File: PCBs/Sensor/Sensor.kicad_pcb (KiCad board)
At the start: 2 copper layers, 35 x 45 mm, 7 parts, among them J1 RJ45, J2 RJ45, U1 ATtiny85-20P

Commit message: added info text
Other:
- board text added: "Laser-Parkour Sensor Rev. 01 © 2024 Manuel König HHN HTWG x42.space"
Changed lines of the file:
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@@
 	)
 	(paper "A4")
+	(title_block
+		(title "Laser-Parkour Sensor")
+		(date "2024-08-24")
+		(rev "01")
+		(company "Manuel König HHN HTWG x42.space")
+	)
 	(layers
 		(0 "F.Cu" signal)
@@
 		(layer "Edge.Cuts")
 	)
+	(gr_text "Laser-Parkour Sensor Rev. 01\n© 2024 Manuel König HHN HTWG\nx42.space "
+		(at 65 92.5 270)
+		(layer "B.SilkS")
+		(effects
+			(font
+				(size 1.5 1.5)
+				(thickness 0.3)
+				(bold yes)
+			)
+			(justify left bottom mirror)
+		)
+	)
 	(segment

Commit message: update footprint
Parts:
- J1, J2: footprint Sensor:WR-MJ Modular Jack Horizontal Shielded w. EMI Panel Finger 8P8C Tab Up -> Library:WR-MJ Modular Jack Horizontal Shielded w. EMI Panel Finger 8P8C Tab Up
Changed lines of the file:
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@@
 		)
 	)
-	(footprint "Sensor:WR-MJ Modular Jack Horizontal Shielded w. EMI Panel Finger 8P8C Tab Up"
+	(footprint "Library:WR-MJ Modular Jack Horizontal Shielded w. EMI Panel Finger 8P8C Tab Up"
 		(layer "F.Cu")
 		(at 76.015 84.705 90)
 		(descr "WR-MJ Modular Jack Horizontal Shielded w. EMI Panel Finger 8P8C Tab Up")
 		(property "Reference" "J2"
-			(at -8.15 -9.015 90)
+			(at 10.1925 -6.485 90)
 			(unlocked yes)
 			(layer "F.SilkS")
@@
 		)
 		(property "Value" "RJ45"
-			(at -8.2325 -6.5575 90)
+			(at 10.11 -4.0275 90)
 			(unlocked yes)
 			(layer "F.Fab")
@@
 			)
 		)
-		(property "Footprint" "Sensor:WR-MJ Modular Jack Horizontal Shielded w. EMI Panel Finger 8P8C Tab Up"
+		(property "Footprint" "Library:WR-MJ Modular Jack Horizontal Shielded w. EMI Panel Finger 8P8C Tab Up"
 			(at 0 0 90)
 			(layer "F.Fab")
@@
 		)
 	)
-	(footprint "Sensor:WR-MJ Modular Jack Horizontal Shielded w. EMI Panel Finger 8P8C Tab Up"
+	(footprint "Library:WR-MJ Modular Jack Horizontal Shielded w. EMI Panel Finger 8P8C Tab Up"
 		(layer "F.Cu")
 		(at 76.015 63.705 90)
 		(descr "WR-MJ Modular Jack Horizontal Shielded w. EMI Panel Finger 8P8C Tab Up")
 		(property "Reference" "J1"
-			(at -8.0675 -8.9725 90)
+			(at 10.1925 -6.485 90)
 			(unlocked yes)
 			(layer "F.SilkS")
@@
 		)
 		(property "Value" "RJ45"
-			(at -8.15 -6.515 90)
+			(at 10.11 -4.0275 90)
 			(unlocked yes)
 			(layer "F.Fab")
@@
 			)
 		)
-		(property "Footprint" "Sensor:WR-MJ Modular Jack Horizontal Shielded w. EMI Panel Finger 8P8C Tab Up"
+		(property "Footprint" "Library:WR-MJ Modular Jack Horizontal Shielded w. EMI Panel Finger 8P8C Tab Up"
 			(at 0 0 90)
 			(layer "F.Fab")

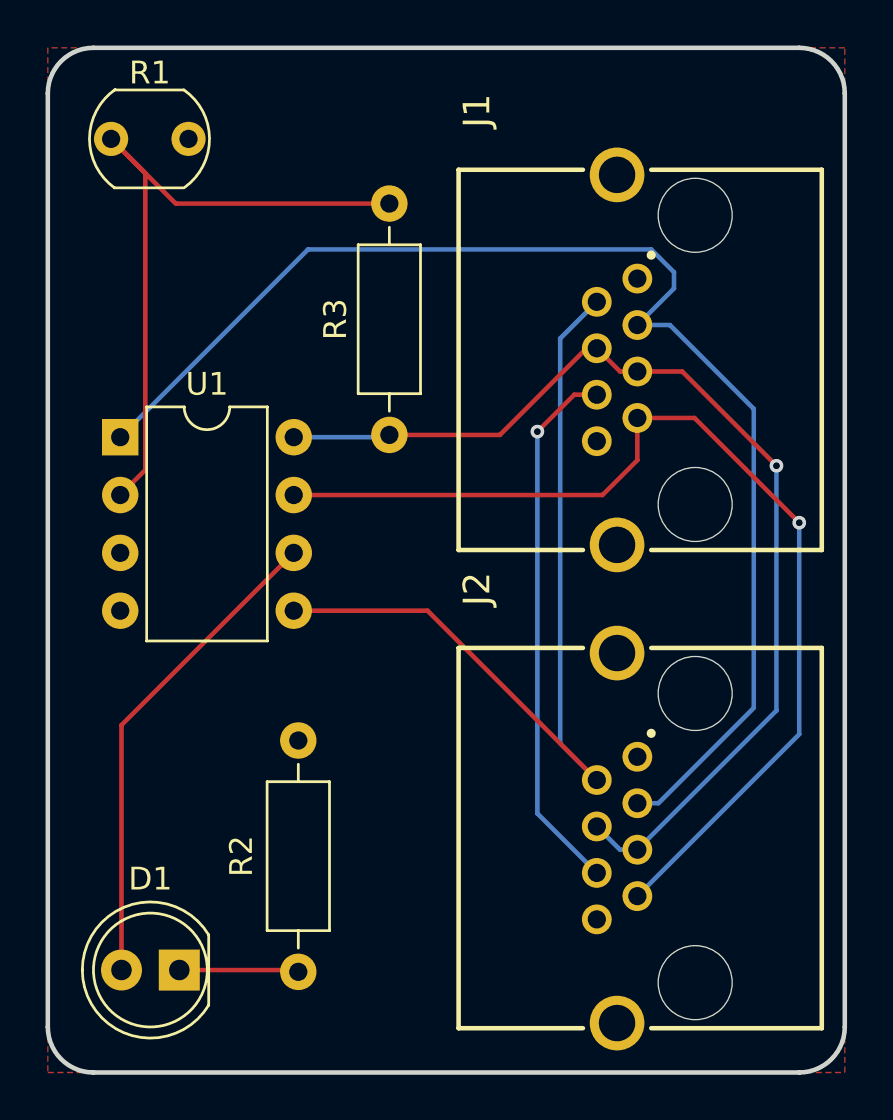
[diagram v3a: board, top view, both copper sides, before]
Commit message: integrate buzzer PCB into Sensor
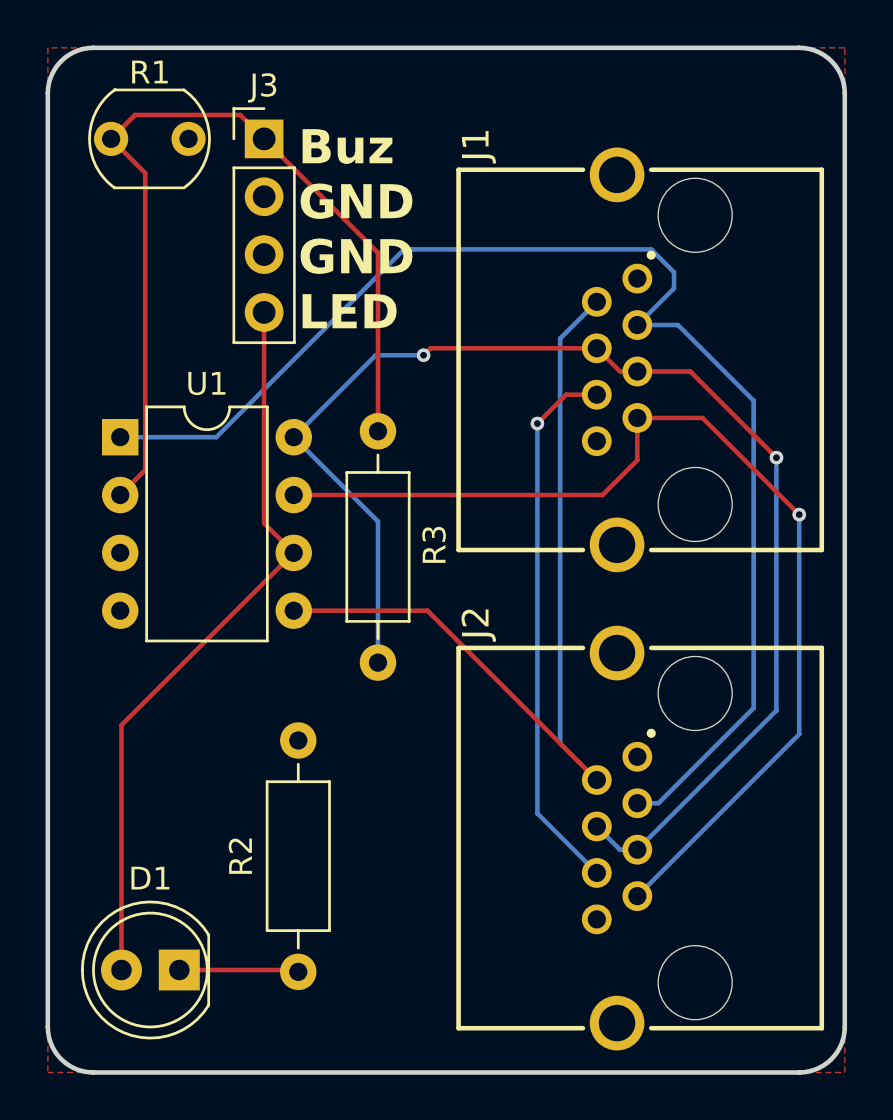
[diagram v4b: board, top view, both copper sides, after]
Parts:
- added J3: Conn_01x04_Pin, Connector_PinHeader_2.54mm:PinHeader_1x04_P2.54mm_Vertical, F.Cu at (59.5, 54.0)
- moved R3 10.0 mm to (64.5, 77.0)
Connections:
- net Net-(D1-A) renamed /out
- net Net-(U1-XTAL1/PB3) renamed /in
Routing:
- net +5V: track 46.5 -> 57.8 mm, vias 1 -> 2
- net /out: track 21.5 -> 32.6 mm
- net /in: track 30.1 -> 39.2 mm
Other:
- board text added: "Buz GND GND LED"

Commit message: Update README
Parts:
- D1: value green -> LED
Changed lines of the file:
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@@
 			)
 		)
-		(property "Value" "green"
+		(property "Value" "LED"
 			(at 1.275 -3.5 0)
 			(layer "F.Fab")

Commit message: added jumper pad
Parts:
- added JP1: Jumper_2_Open, Jumper:SolderJumper-2_P1.3mm_Open_TrianglePad1.0x1.5mm, B.Cu at (56.8, 83.5)
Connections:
- U1 pad 3: unconnected-(U1-XTAL2/PB4-Pad3) -> Net-(JP1-A)
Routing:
- net Net-(JP1-B): track 24.0 -> 38.0 mm
- net Net-(JP1-A): track 0.00 -> 12.5 mm
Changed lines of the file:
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@@
 	(net 2 "/out")
 	(net 3 "+5V")
-	(net 4 "Net-(J1-Pad6)")
+	(net 4 "Net-(JP1-B)")
 	(net 5 "GND")
 	(net 6 "/SDA")
@@
 	(net 8 "/SCL")
 	(net 9 "/in")
-	(net 10 "unconnected-(U1-XTAL2{slash}PB4-Pad3)")
+	(net 10 "Net-(JP1-A)")
 	(footprint "OptoDevice:R_LDR_5.1x4.3mm_P3.4mm_Vertical"
 		(layer "F.Cu")
@@
 			(layers "*.Cu" "*.Mask")
 			(remove_unused_layers no)
-			(net 4 "Net-(J1-Pad6)")
+			(net 4 "Net-(JP1-B)")
 			(pintype "passive")
 			(solder_mask_margin 0.1016)
@@
 			(layers "*.Cu" "*.Mask")
 			(remove_unused_layers no)
-			(net 4 "Net-(J1-Pad6)")
+			(net 4 "Net-(JP1-B)")
 			(pintype "passive")
 			(solder_mask_margin 0.1016)
@@
 			(layers "*.Cu" "*.Mask")
 			(remove_unused_layers no)
-			(net 10 "unconnected-(U1-XTAL2{slash}PB4-Pad3)")
+			(net 10 "Net-(JP1-A)")
 			(pinfunction "XTAL2/PB4")
-			(pintype "bidirectional+no_connect")
+			(pintype "bidirectional")
 		)
 		(pad "4" thru_hole oval
@@
 			(rotate
 				(xyz 0 0 0)
+			)
+		)
+	)
+	(footprint "Jumper:SolderJumper-2_P1.3mm_Open_TrianglePad1.0x1.5mm"
+		(layer "B.Cu")
+		(at 56.775 83.5)
+		(descr "SMD Solder Jumper, 1x1.5mm Triangular Pads, 0.3mm gap, open")
+		(tags "solder jumper open")
+		(property "Reference" "JP1"
+			(at 0 1.8 360)
+			(layer "B.SilkS")
+			(effects
+				(font
+					(size 1 1)
+					(thickness 0.15)
+				)
+				(justify mirror)
+			)
+		)
+		(property "Value" "Jumper_2_Open"
+			(at 0 -1.9 360)
+			(layer "B.Fab")
+			(effects
+				(font
+					(size 1 1)
+					(thickness 0.15)
+				)
+				(justify mirror)
+			)
+		)
+		(property "Footprint" "Jumper:SolderJumper-2_P1.3mm_Open_TrianglePad1.0x1.5mm"
+			(at 0 0 180)
+			(unlocked yes)
+			(layer "B.Fab")
+			(hide yes)
+			(effects
+				(font
+					(size 1.27 1.27)
+					(thickness 0.15)
+				)
+				(justify mirror)
+			)
+		)
+		(property "Datasheet" ""
+			(at 0 0 180)
+			(unlocked yes)
+			(layer "B.Fab")
+			(hide yes)
+			(effects
+				(font
+					(size 1.27 1.27)
+					(thickness 0.15)
+				)
+				(justify mirror)
+			)
+		)
+		(property "Description" "Jumper, 2-pole, open"
+			(at 0 0 180)
+			(unlocked yes)
+			(layer "B.Fab")
+			(hide yes)
+			(effects
+				(font
+					(size 1.27 1.27)
+					(thickness 0.15)
+				)
+				(justify mirror)
+			)
+		)
+		(property ki_fp_filters "Jumper* TestPoint*2Pads* TestPoint*Bridge*")
+		(sheetname "Root")
+		(sheetfile "Sensor.kicad_sch")
+		(zone_connect 1)
+		(attr exclude_from_pos_files)
+		(fp_line
+			(start -1.4 -1)
+			(end 1.4 -1)
+			(stroke
+				(width 0.12)
+				(type solid)
+			)
+			(layer "B.SilkS")
+		)
+		(fp_line
+			(start -1.4 1)
+			(end -1.4 -1)
+			(stroke
+				(width 0.12)
+				(type solid)
+			)
+			(layer "B.SilkS")
+		)
+		(fp_line
+			(start 1.4 -1)
+			(end 1.4 1)
+			(stroke
+				(width 0.12)
+				(type solid)
+			)
+			(layer "B.SilkS")
+		)
+		(fp_line
+			(start 1.4 1)
+			(end -1.4 1)
+			(stroke
+				(width 0.12)
+				(type solid)
+			)
+			(layer "B.SilkS")
+		)
+		(fp_line
+			(start -1.65 -1.25)
+			(end -1.65 1.25)
+			(stroke
+				(width 0.05)
+				(type solid)
+			)
+			(layer "B.CrtYd")
+		)
+		(fp_line
+			(start -1.65 -1.25)
+			(end 1.65 -1.25)
+			(stroke
+				(width 0.05)
+				(type solid)
+			)
+			(layer "B.CrtYd")
+		)
+		(fp_line
+			(start 1.65 1.25)
+			(end -1.65 1.25)
+			(stroke
+				(width 0.05)
+				(type solid)
+			)
+			(layer "B.CrtYd")
+		)
+		(fp_line
+			(start 1.65 1.25)
+			(end 1.65 -1.25)
+			(stroke
+				(width 0.05)
+				(type solid)
+			)
+			(layer "B.CrtYd")
+		)
+		(pad "1" smd custom
+			(at -0.725 0)
+			(size 0.3 0.3)
+			(layers "B.Cu" "B.Mask")
+			(net 10 "Net-(JP1-A)")
+			(pinfunction "A")
+			(pintype "passive")
+			(zone_connect 2)
+			(thermal_bridge_angle 45)
+			(options
+				(clearance outline)
+				(anchor rect)
+			)
+			(primitives
+				(gr_poly
+					(pts
+						(xy 1 0) (xy 0.5 -0.75) (xy -0.5 -0.75) (xy -0.5 0.75) (xy 0.5 0.75)
+					)
+					(width 0)
+					(fill yes)
+				)
+			)
+		)
+		(pad "2" smd custom
+			(at 0.725 0)
+			(size 0.3 0.3)
+			(layers "B.Cu" "B.Mask")
+			(net 4 "Net-(JP1-B)")
+			(pinfunction "B")
+			(pintype "passive")
+			(zone_connect 2)
+			(thermal_bridge_angle 45)
+			(options
+				(clearance outline)
+				(anchor rect)
+			)
+			(primitives
+				(gr_poly
+					(pts
+						(xy 0.5 -0.75) (xy -0.65 -0.75) (xy -0.15 0) (xy -0.65 0.75) (xy 0.5 0.75)
+					)
+					(width 0)
+					(fill yes)
+				)
 			)
 		)
@@
 	)
 	(segment
+		(start 57.5 83.5)
+		(end 71.375 83.5)
+		(width 0.2)
+		(layer "B.Cu")
+		(net 4)
+	)
+	(segment
+		(start 71.375 83.5)
+		(end 71.5 83.625)
+		(width 0.2)
+		(layer "B.Cu")
+		(net 4)
+	)
+	(segment
 		(start 71.5 83.625)
 		(end 74.11 86.235)
@@
 		(net 9)
 	)
+	(segment
+		(start 53.18 72.18)
+		(end 56.05 75.05)
+		(width 0.2)
+		(layer "B.Cu")
+		(net 10)
+	)
+	(segment
+		(start 56.05 75.05)
+		(end 56.05 83.5)
+		(width 0.2)
+		(layer "B.Cu")
+		(net 10)
+	)
 	(zone

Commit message: update sensor
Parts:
- added C1: 0.1μ, Capacitor_THT:C_Disc_D3.0mm_W1.6mm_P2.50mm, F.Cu at (66.0, 64.5)
- added J4: RJ45, Library:WR-MJ Modular Jack Horizontal Shielded w. EMI Panel Finger 8P8C Tab Up, F.Cu at (58.0, 78.5)
- added JP2: Jumper_2_Open, Jumper:SolderJumper-2_P1.3mm_Open_RoundedPad1.0x1.5mm, B.Cu at (58.5, 59.5)
- J1: value RJ45 -> Conn_01x04_Pin; footprint Library:WR-MJ Modular Jack Horizontal Shielded w. EMI Panel Finger 8P8C Tab Up -> Connector_PinHeader_2.54mm:PinHeader_1x04_P2.54mm_Vertical
- J3: value Conn_01x04_Pin -> RJ45; footprint Connector_PinHeader_2.54mm:PinHeader_1x04_P2.54mm_Vertical -> Library:WR-MJ Modular Jack Horizontal Shielded w. EMI Panel Finger 8P8C Tab Up
- JP1: value Jumper_2_Open -> Jumper_2_Bridged; footprint Jumper:SolderJumper-2_P1.3mm_Open_TrianglePad1.0x1.5mm -> Jumper:SolderJumper-2_P1.3mm_Bridged_RoundedPad1.0x1.5mm
- R1: value LDR07 -> 10k; footprint OptoDevice:R_LDR_5.1x4.3mm_P3.4mm_Vertical -> Resistor_THT:R_Axial_DIN0207_L6.3mm_D2.5mm_P10.16mm_Horizontal
- R2: value 220 -> LDR07; footprint Resistor_THT:R_Axial_DIN0207_L6.3mm_D2.5mm_P10.16mm_Horizontal -> OptoDevice:R_LDR_5.1x4.3mm_P3.4mm_Vertical
- R3: value 10k -> 220
- moved J3 35.6 mm to (77.0, 85.0), turned to 90 degrees
- moved JP1 28.9 mm to (67.2, 56.5)
- moved R2 28.9 mm to (70.0, 53.0), turned to 180 degrees
- moved R1 20.2 mm to (72.9, 53.0)
- moved J2 19.7 mm to (77.0, 65.0)
- moved J1 17.6 mm to (62.5, 52.5), turned to -90 degrees
- moved R3 17.3 mm to (57.4, 92.8), turned to 0 degrees
- moved U1 14.2 mm to (62.8, 56.7), turned to -90 degrees
- moved D1 3.59 mm to (53.0, 92.8), turned to 90 degrees
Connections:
- J1 pad 2: /SDA -> GND
- J1 pad 3: /Reset -> /in
- J1 pad 4: +5V -> /out
- J2 pad 2: /SDA -> /SDA0
- J2 pad 3: /Reset -> Net-(JP1-B)
- J2 pad 4: +5V -> +3.3V
- J2 pad 5: +5V -> +3.3V
- J2 pad 6: Net-(JP1-B) -> Net-(JP2-B)
- J2 pad 7: /SCL -> /SCL0
- J3 pad 1: /in -> GND
- J3 pad 2: GND -> /SDA0
- J3 pad 3: GND -> Net-(JP1-B)
- J3 pad 4: /out -> +3.3V
- JP1 pad 1: Net-(JP1-A) -> /AT_RS
- R1 pad 2: GND -> +3.3V
- R2 pad 1: GND -> /in
- R2 pad 2: Net-(D1-K) -> GND
- R3 pad 1: +5V -> Net-(D1-K)
- R3 pad 2: /in -> GND
- U1 pad 1: /Reset -> /AT_RS
- U1 pad 3: Net-(JP1-A) -> /FU
- U1 pad 5: /SDA -> /SDA0
- U1 pad 7: /SCL -> /SCL0
- U1 pad 8: +5V -> +3.3V
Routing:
- net +3.3V: track 0.00 -> 86.9 mm, vias 0 -> 3
- net /SCL0: track 0.00 -> 64.6 mm, vias 0 -> 3
- net /Reset: track 58.0 -> 0.00 mm
- net Net-(JP1-B): track 38.0 -> 95.9 mm, vias 1 -> 2
- net +5V: track 57.8 -> 0.00 mm, vias 2 -> 0
- net /SDA0: track 0.00 -> 57.6 mm, vias 0 -> 2
- net Net-(JP2-B): track 0.00 -> 56.8 mm, vias 0 -> 3
- net /SCL: track 46.1 -> 0.00 mm, vias 1 -> 0
- net /SDA: track 39.1 -> 0.00 mm
- net /in: track 39.2 -> 19.9 mm
- net /out: track 32.6 -> 47.9 mm
- net Net-(JP1-A): track 12.5 -> 0.00 mm
- net /AT_RS: track 0.00 -> 3.78 mm
- net /FU: track 0.00 -> 2.85 mm
- net Net-(D1-K): track 5.26 -> 4.43 mm
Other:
- board text added: "BUZ LED GND"
- board text removed: "Buz GND GND LED"
